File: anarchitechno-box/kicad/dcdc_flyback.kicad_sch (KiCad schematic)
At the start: 44 parts, among them J7 Screw_Terminal_01x02, U1 EC5DAW-24S05N, U18 ADPL54203ES8E#PBF, U19 750311564, U22 LMR54410FDBVR, U3 LMR54410FDBVR

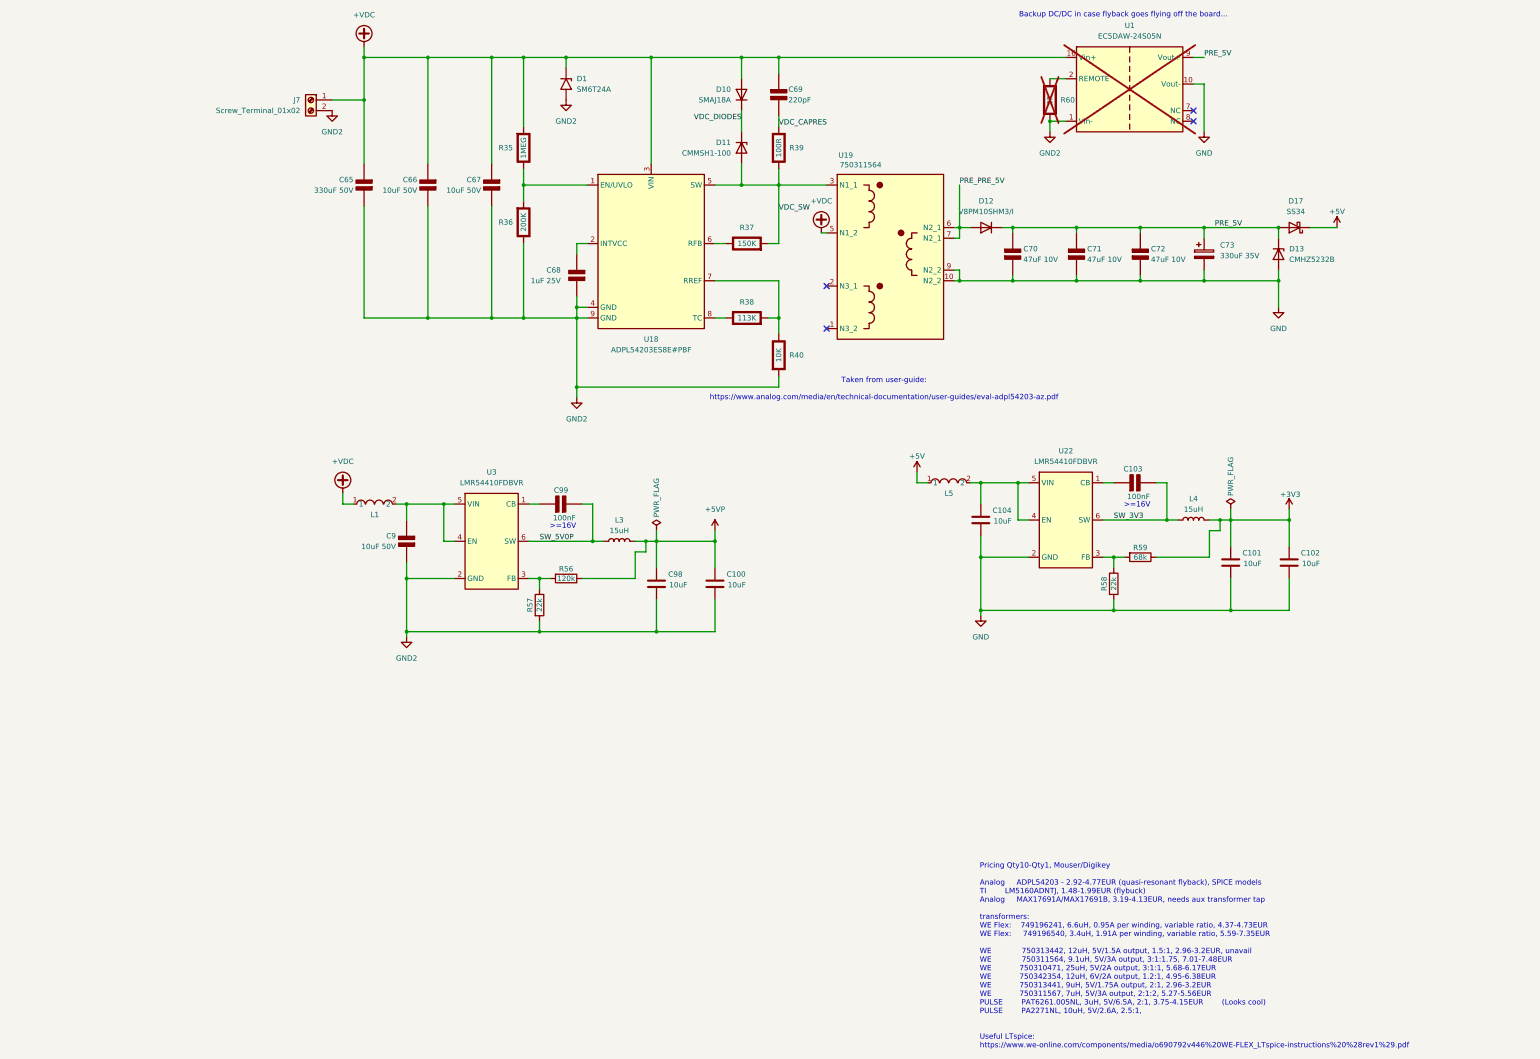
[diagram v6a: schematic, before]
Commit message: Schematic & PCB changes: - Cleaned up unnecessary electrolytic input capacitor flyback - Removed dual diode rectification on 5V, increased output capacitors - Feedback resistors DC/DCs set, enlarged for JLC basic parts - Sweep through schematic to consolidate caps to JLC basic parts (see list schematic front page) - Midi OUTPUT added (please check schematic) - Wiznet W5500 schematic reworked to RJ45 reference schematic: https://docs.wiznet.io/assets/files/w5500_sch_v110_use_mag_-dfff8bbb103d13be4f25cd2b2f8b950d.pdf - Replaced ethernet jack to HR911105A - Crystals chosen for W5500 and RP2350B (according to reference), 15pF load caps. - RS485 driver changed to SP3485EN for 3.3V operation - Replaced RS485 bus connectors with 2x RJ45s for passthrough - Groove connector replaced with JST XH 2mm - Added LCSC part numbers for various components in the schematic
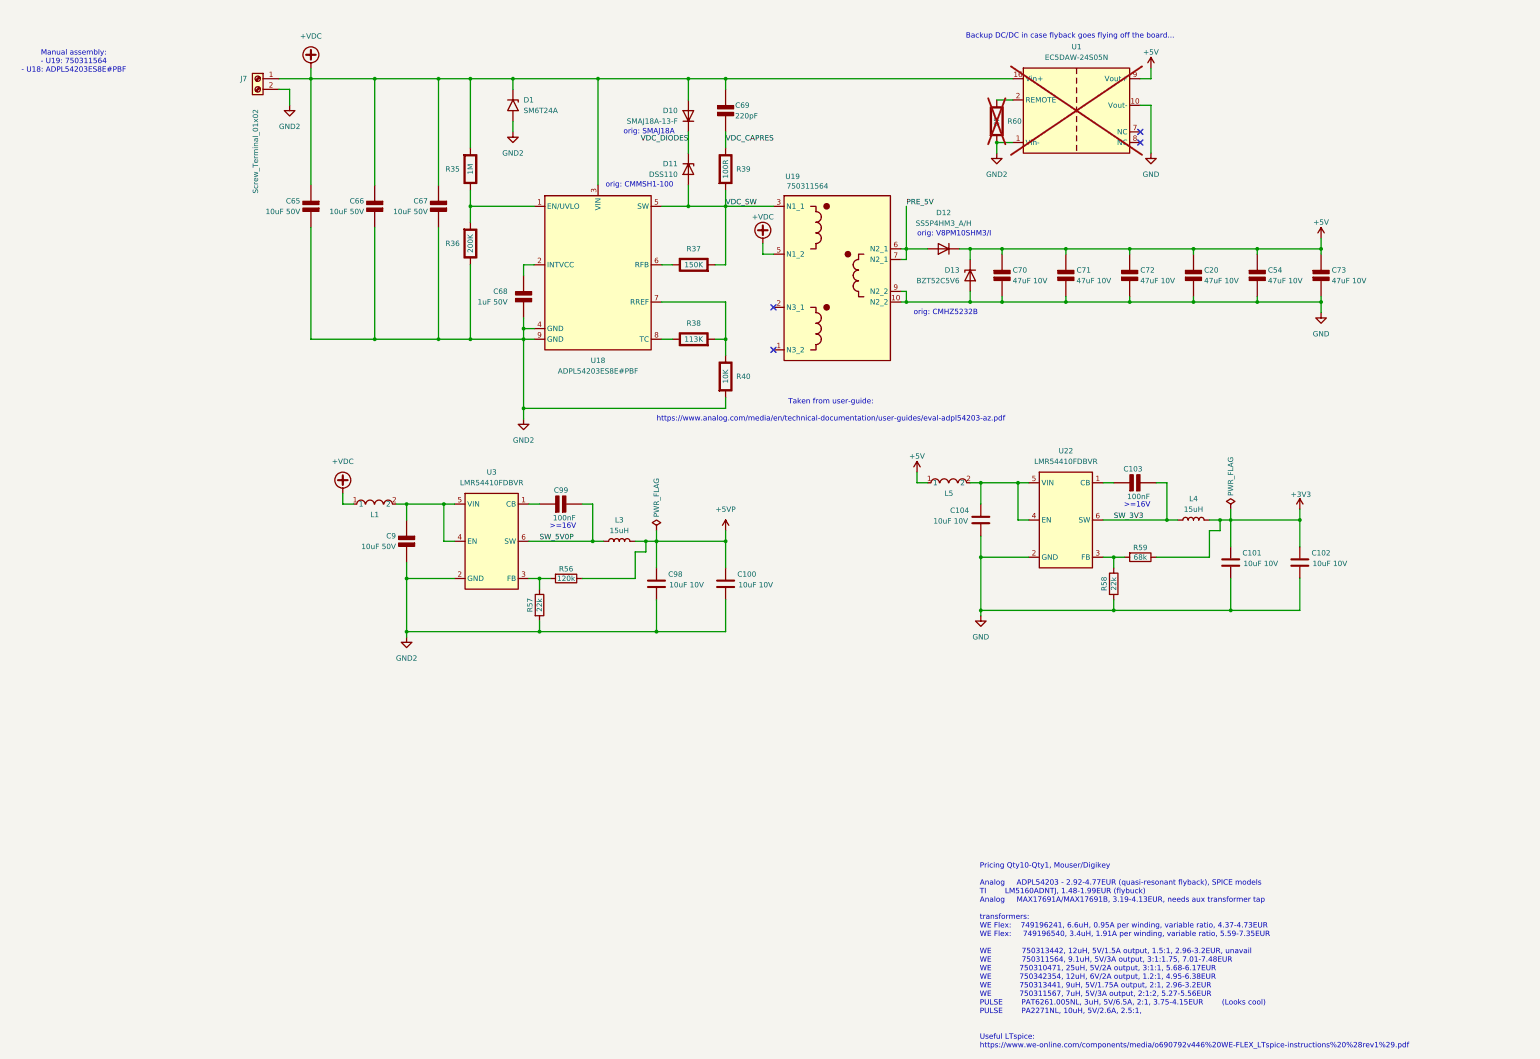
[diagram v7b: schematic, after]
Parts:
- removed C73: 330uF 35V, symbol Device:C_Polarized
- removed D17: SS34, Diode_SMD:D_SMA, symbol Diode:SS34
- added C20, C54, C73: 47uF 10V, Capacitor_SMD:C_1210_3225Metric, symbol PCM_Elektuur:C
- C100, C101, C102, C104, C98: value 10uF -> 10uF 10V; Digi-Key_PN 311-1344-1-ND -> (none); LCSC Part (none) -> C19702
- C65: value 330uF 50V -> 10uF 50V; footprint (none) -> Capacitor_SMD:C_1206_3216Metric; LCSC Part (none) -> C13585
- C66, C67, C9: footprint Capacitor_SMD:C_1210_3225Metric -> Capacitor_SMD:C_1206_3216Metric; LCSC Part (none) -> C13585
- C68: value 1uF 25V -> 1uF 50V; footprint Capacitor_SMD:C_0805_2012Metric -> Capacitor_SMD:C_0603_1608Metric; LCSC Part (none) -> C15849
- C69: LCSC Part (none) -> C107145; MPN (none) -> CC0805KRX7R9BB221
- C70, C71, C72: LCSC Part (none) -> C96123
- D1: LCSC Part (none) -> C47021062
- D10: value SMAJ18A -> SMAJ18A-13-F; LCSC Part (none) -> C134965; MPN SMAJ18A -> SMAJ18A-13-F
- D11: value CMMSH1-100 -> DSS110; LCSC Part (none) -> C49023411; MPN CMMSH1-100 -> DSS110
- D12: value V8PM10SHM3/I -> SS5P4HM3_A/H; LCSC Part (none) -> C467999; MPN V8PM10SHM3/I -> SS5P4HM3_A/H
- D13: value CMHZ5232B -> BZT52C5V6; LCSC Part (none) -> C2827906; MPN CMHZ5232B -> BZT52C5V6
- R35: value 1MEG -> 1M; LCSC Part (none) -> C22935
- R36: LCSC Part (none) -> C25811
- R37: LCSC Part (none) -> C22807
- R38: LCSC Part (none) -> C321689
- R39: LCSC Part (none) -> C22775
- R40: LCSC Part (none) -> C25804
- R56: footprint Resistor_SMD:R_0402_1005Metric -> Resistor_SMD:R_0603_1608Metric; LCSC Part (none) -> C25808
- R57, R58: LCSC Part (none) -> C25768
- R59: footprint Resistor_SMD:R_0402_1005Metric -> Resistor_SMD:R_0603_1608Metric; LCSC Part (none) -> C23231
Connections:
- net PRE_PRE_5V is gone; now on net PRE_5V: D12.1 (A), D12.2 (A), U19.6 (N2_1), U19.7 (N2_1)
- net +5V: now also C70.1 (+), C71.1 (+), C72.1 (+), D12.3 (K), D13.1 (K), U1.9 (Vout+), C20.1 (+), C54.1 (+), C73.1 (+)
- net GND: now also C20.2 (-), C54.2 (-), C73.2 (-)
- net PRE_5V: no longer C70.1 (+), C71.1 (+), C72.1 (+), D12.3 (K), D13.1 (K), U1.9 (Vout+)
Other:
- note added: "Manual assembly: - U19: 750311564 - U18: ADPL54203ES8E#PBF"
- note added: "orig: CMHZ5232B"
- note added: "orig: CMMSH1-100"
- note added: "orig: SMAJ18A"
- note added: "orig: V8PM10SHM3/I"
- moved on the sheet: C100, C102, C66, C67, C68, C69, C70, C71, C72, D1, D10, D11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

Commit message: BOM nagelopen, bestelklaar.
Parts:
- J7: footprint TerminalBlock_Phoenix:TerminalBlock_Phoenix_PT-1,5-2-5.0-H_1x02_P5.00mm_Horizontal -> TerminalBlock_Phoenix:TerminalBlock_Phoenix_MKDS-1,5-2-5.08_1x02_P5.08mm_Horizontal; LCSC Part (none) -> C395868
- L3, L4: footprint parts:CENKER_CKCS5040 -> parts:PSPMAA0402; LCSC Part C5291847 -> C5273841
- R39: LCSC Part C22775 -> C17901
- U18: LCSC Part (none) -> C29100686
- U19: LCSC Part (none) -> C17454010
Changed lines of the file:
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@@
 			)
 		)
+		(property "LCSC Part" "C17454010"
+			(at 143.51 57.15 0)
+			(effects
+				(font
+					(size 1.27 1.27)
+				)
+				(hide yes)
+			)
+		)
 		(pin "2"
 		)
@@
 			)
 		)
-		(property "LCSC Part" "C22775"
+		(property "LCSC Part" "C17901"
 			(at 129.54 50.8 0)
 			(effects
@@
 			)
 		)
+		(property "LCSC Part" "C29100686"
+			(at 86.36 54.61 0)
+			(effects
+				(font
+					(size 1.27 1.27)
+				)
+				(hide yes)
+			)
+		)
 		(pin "4"
 		)
@@
 			)
 		)
-		(property "Footprint" "parts:CENKER_CKCS5040"
+		(property "Footprint" "parts:PSPMAA0402"
 			(at 104.14 139.7 0)
 			(effects
@@
 			)
 		)
-		(property "LCSC Part" "C5291847"
+		(property "LCSC Part" "C5273841"
 			(at 104.14 139.7 90)
 			(effects
@@
 			)
 		)
-		(property "Footprint" "TerminalBlock_Phoenix:TerminalBlock_Phoenix_PT-1,5-2-5.0-H_1x02_P5.00mm_Horizontal"
+		(property "Footprint" "TerminalBlock_Phoenix:TerminalBlock_Phoenix_MKDS-1,5-2-5.08_1x02_P5.08mm_Horizontal"
 			(at 17.78 29.21 0)
 			(effects
@@
 			)
 		)
+		(property "LCSC Part" "C395868"
+			(at 17.78 29.21 0)
+			(effects
+				(font
+					(size 1.27 1.27)
+				)
+				(hide yes)
+			)
+		)
 		(pin "1"
 		)
@@
 			)
 		)
-		(property "Footprint" "parts:CENKER_CKCS5040"
+		(property "Footprint" "parts:PSPMAA0402"
 			(at 241.3 134.62 0)
 			(effects
@@
 			)
 		)
-		(property "LCSC Part" "C5291847"
+		(property "LCSC Part" "C5273841"
 			(at 241.3 134.62 90)
 			(effects
